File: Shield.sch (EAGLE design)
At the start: 80 parts

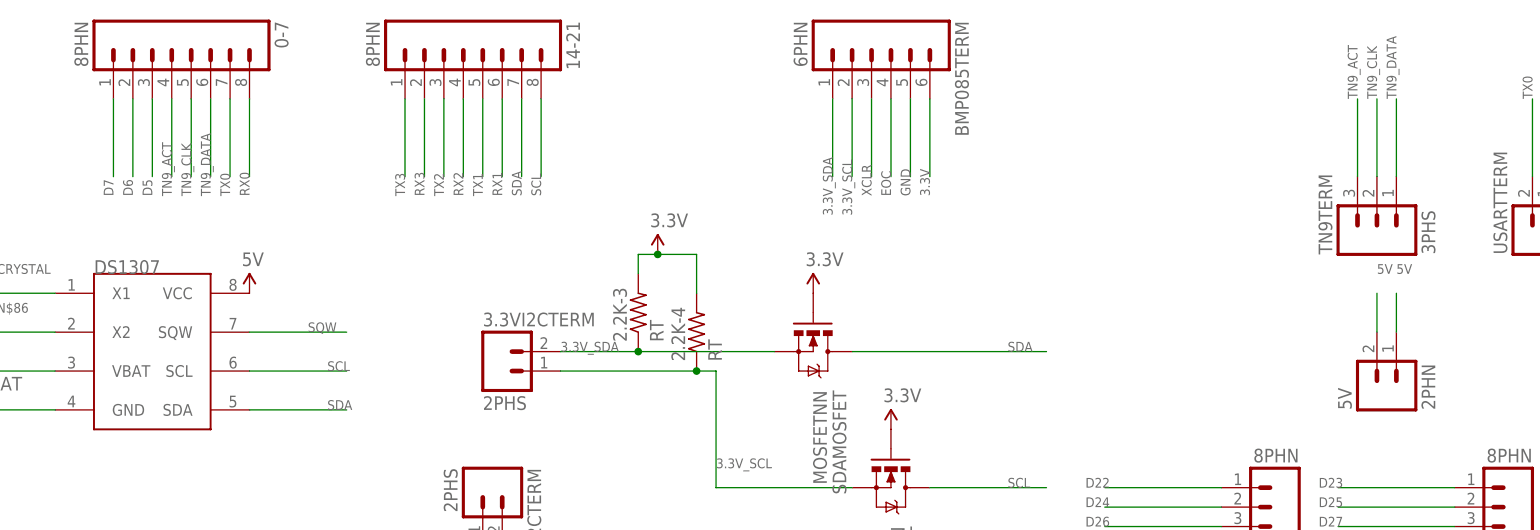
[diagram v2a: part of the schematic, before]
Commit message: Added middle screw terminals
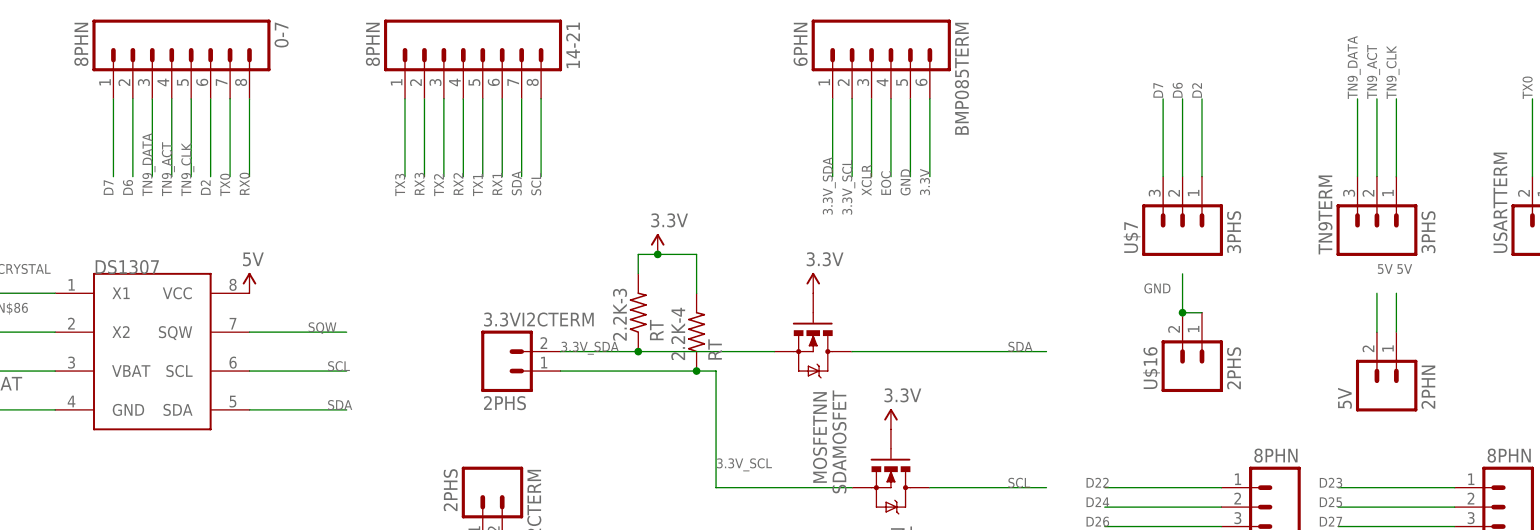
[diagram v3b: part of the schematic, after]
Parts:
- added U$16: 2PHS, LEMS:2PHS
- added U$7: 3PHS, LEMS:3PHS
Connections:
- removed net D5: 0-7.3
- new net D2: 0-7.6, U$7.1
- net D6: now also U$7.2
- net D7: now also U$7.3
- net GND: now also U$16.1, U$16.2
- net TN9_ACT: now also TN9TERM.2; no longer TN9TERM.3
- net TN9_CLK: now also TN9TERM.1; no longer TN9TERM.2
- net TN9_DATA: now also 0-7.3, TN9TERM.3; no longer 0-7.6, TN9TERM.1
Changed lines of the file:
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@@
 <part name="SCHOTTKY" library="adafruit" deviceset="SCHOTTKY-DIODE" device="DO41"/>
 <part name="ZENER" library="LEMS" deviceset="1N4004" device=""/>
+<part name="U$7" library="LEMS" deviceset="3PH" device="S"/>
+<part name="U$16" library="LEMS" deviceset="2PH" device="S"/>
 </parts>
 <sheets>
@@
 <instance part="SCHOTTKY" gate="G$1" x="340.36" y="83.82"/>
 <instance part="ZENER" gate="1" x="332.74" y="81.28" rot="R90"/>
+<instance part="U$7" gate="G$1" x="261.62" y="228.6" rot="R90"/>
+<instance part="U$16" gate="G$1" x="261.62" y="210.82" rot="R90"/>
 </instances>
 <busses>
@@
 <wire x1="327.66" y1="78.74" x2="327.66" y2="81.28" width="0.1524" layer="91"/>
 <wire x1="327.66" y1="81.28" x2="312.42" y2="81.28" width="0.1524" layer="91"/>
+</segment>
+<segment>
+<pinref part="U$16" gate="G$1" pin="1"/>
+<pinref part="U$16" gate="G$1" pin="2"/>
+<wire x1="264.16" y1="215.9" x2="261.62" y2="215.9" width="0.1524" layer="91"/>
+<wire x1="261.62" y1="220.98" x2="261.62" y2="215.9" width="0.1524" layer="91"/>
+<junction x="261.62" y="215.9"/>
+<label x="256.54" y="218.44" size="1.27" layer="95"/>
 </segment>
 </net>
@@
 <label x="121.92" y="231.14" size="1.27" layer="95" rot="R90"/>
 </segment>
+<segment>
+<pinref part="U$7" gate="G$1" pin="3"/>
+<wire x1="259.08" y1="233.68" x2="259.08" y2="243.84" width="0.1524" layer="91"/>
+<label x="259.08" y="243.84" size="1.27" layer="95" rot="R90"/>
+</segment>
 </net>
 <net name="D6" class="0">
@@
 <label x="124.46" y="231.14" size="1.27" layer="95" rot="R90"/>
 </segment>
-</net>
-<net name="D5" class="0">
+<segment>
+<pinref part="U$7" gate="G$1" pin="2"/>
+<wire x1="261.62" y1="233.68" x2="261.62" y2="243.84" width="0.1524" layer="91"/>
+<label x="261.62" y="243.84" size="1.27" layer="95" rot="R90"/>
+</segment>
+</net>
+<net name="TN9_ACT" class="0">
+<segment>
+<pinref part="0-7" gate="G$1" pin="4"/>
+<wire x1="129.54" y1="243.84" x2="129.54" y2="233.68" width="0.1524" layer="91"/>
+<label x="129.54" y="231.14" size="1.27" layer="95" rot="R90"/>
+</segment>
+<segment>
+<pinref part="TN9TERM" gate="G$1" pin="2"/>
+<wire x1="287.02" y1="233.68" x2="287.02" y2="243.84" width="0.1524" layer="91"/>
+<label x="287.02" y="243.84" size="1.27" layer="95" rot="R90"/>
+</segment>
+</net>
+<net name="TN9_CLK" class="0">
+<segment>
+<pinref part="0-7" gate="G$1" pin="5"/>
+<wire x1="132.08" y1="243.84" x2="132.08" y2="233.68" width="0.1524" layer="91"/>
+<label x="132.08" y="231.14" size="1.27" layer="95" rot="R90"/>
+</segment>
+<segment>
+<pinref part="TN9TERM" gate="G$1" pin="1"/>
+<wire x1="289.56" y1="233.68" x2="289.56" y2="243.84" width="0.1524" layer="91"/>
+<label x="289.56" y="243.84" size="1.27" layer="95" rot="R90"/>
+</segment>
+</net>
+<net name="TN9_DATA" class="0">
 <segment>
 <pinref part="0-7" gate="G$1" pin="3"/>
@@
 <label x="127" y="231.14" size="1.27" layer="95" rot="R90"/>
 </segment>
-</net>
-<net name="TN9_ACT" class="0">
-<segment>
-<pinref part="0-7" gate="G$1" pin="4"/>
-<wire x1="129.54" y1="243.84" x2="129.54" y2="233.68" width="0.1524" layer="91"/>
-<label x="129.54" y="231.14" size="1.27" layer="95" rot="R90"/>
-</segment>
 <segment>
 <pinref part="TN9TERM" gate="G$1" pin="3"/>
 <wire x1="284.48" y1="233.68" x2="284.48" y2="243.84" width="0.1524" layer="91"/>
 <label x="284.48" y="243.84" size="1.27" layer="95" rot="R90"/>
-</segment>
-</net>
-<net name="TN9_CLK" class="0">
-<segment>
-<pinref part="0-7" gate="G$1" pin="5"/>
-<wire x1="132.08" y1="243.84" x2="132.08" y2="233.68" width="0.1524" layer="91"/>
-<label x="132.08" y="231.14" size="1.27" layer="95" rot="R90"/>
-</segment>
-<segment>
-<pinref part="TN9TERM" gate="G$1" pin="2"/>
-<wire x1="287.02" y1="233.68" x2="287.02" y2="243.84" width="0.1524" layer="91"/>
-<label x="287.02" y="243.84" size="1.27" layer="95" rot="R90"/>
-</segment>
-</net>
-<net name="TN9_DATA" class="0">
-<segment>
-<pinref part="0-7" gate="G$1" pin="6"/>
-<wire x1="134.62" y1="243.84" x2="134.62" y2="233.68" width="0.1524" layer="91"/>
-<label x="134.62" y="231.14" size="1.27" layer="95" rot="R90"/>
-</segment>
-<segment>
-<pinref part="TN9TERM" gate="G$1" pin="1"/>
-<wire x1="289.56" y1="233.68" x2="289.56" y2="243.84" width="0.1524" layer="91"/>
-<label x="289.56" y="243.84" size="1.27" layer="95" rot="R90"/>
 </segment>
 </net>
@@
 </segment>
 </net>
+<net name="D2" class="0">
+<segment>
+<pinref part="0-7" gate="G$1" pin="6"/>
+<wire x1="134.62" y1="243.84" x2="134.62" y2="233.68" width="0.1524" layer="91"/>
+<label x="134.62" y="231.14" size="1.27" layer="95" rot="R90"/>
+</segment>
+<segment>
+<pinref part="U$7" gate="G$1" pin="1"/>
+<wire x1="264.16" y1="233.68" x2="264.16" y2="243.84" width="0.1524" layer="91"/>
+<label x="264.16" y="243.84" size="1.27" layer="95" rot="R90"/>
+</segment>
+</net>

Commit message: Minor Spacing Changes
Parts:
- renumbered 1 to 0.5, 6.8UF-T to 10UF-T
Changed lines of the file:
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@@
 <part name="GND18" library="LEMS" deviceset="GND" device=""/>
 <part name="GND19" library="LEMS" deviceset="GND" device=""/>
-<part name="6.8UF-T" library="LEMS" deviceset="CE" device="S"/>
-<part name="1" library="LEMS" deviceset="R" device="T"/>
+<part name="10UF-T" library="LEMS" deviceset="CE" device="S"/>
+<part name="0.5" library="LEMS" deviceset="R" device="T"/>
 <part name="GND20" library="LEMS" deviceset="GND" device=""/>
 <part name="PWRSWTCH" library="LEMS" deviceset="SWITCHSPDT" device="N"/>
@@
 <instance part="GND18" gate="1" x="251.46" y="27.94"/>
 <instance part="GND19" gate="1" x="215.9" y="43.18" rot="R270"/>
-<instance part="6.8UF-T" gate="G$1" x="246.38" y="71.12" rot="R90"/>
-<instance part="1" gate="G$1" x="256.54" y="71.12" rot="R180"/>
+<instance part="10UF-T" gate="G$1" x="246.38" y="71.12" rot="R90"/>
+<instance part="0.5" gate="G$1" x="256.54" y="71.12" rot="R180"/>
 <instance part="GND20" gate="1" x="264.16" y="71.12" rot="R90"/>
 <instance part="PWRSWTCH" gate="G$1" x="284.48" y="40.64"/>
@@
 </segment>
 <segment>
-<pinref part="1" gate="G$1" pin="1"/>
+<pinref part="0.5" gate="G$1" pin="1"/>
 <pinref part="GND20" gate="1" pin="GND"/>
 </segment>
@@
 <net name="N$7" class="0">
 <segment>
-<pinref part="6.8UF-T" gate="G$1" pin="2"/>
-<pinref part="1" gate="G$1" pin="2"/>
+<pinref part="10UF-T" gate="G$1" pin="2"/>
+<pinref part="0.5" gate="G$1" pin="2"/>
 </segment>
 </net>
@@
 <wire x1="243.84" y1="48.26" x2="243.84" y2="53.34" width="0.1524" layer="91"/>
 <junction x="243.84" y="53.34"/>
-<pinref part="6.8UF-T" gate="G$1" pin="1"/>
+<pinref part="10UF-T" gate="G$1" pin="1"/>
 <wire x1="243.84" y1="71.12" x2="243.84" y2="63.5" width="0.1524" layer="91"/>
 <junction x="243.84" y="63.5"/>

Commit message: Ready for Quantity Manufacturing
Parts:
- 4.7K: value RESISTORT -> RN; device LEMS:RESISTORT -> LEMS:RN
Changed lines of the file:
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@@
 <part name="OPA2TERM" library="LEMS" deviceset="3PH" device="N"/>
 <part name="DALLASTERM" library="LEMS" deviceset="3PH" device="S"/>
-<part name="4.7K" library="LEMS" deviceset="RESISTOR" device="T"/>
+<part name="4.7K" library="LEMS" deviceset="R" device="N"/>
 <part name="GND17" library="LEMS" deviceset="GND" device=""/>
 <part name="4.5VTERM" library="LEMS" deviceset="2PH" device="S"/>
